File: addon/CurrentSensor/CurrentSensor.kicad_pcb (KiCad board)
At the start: 2 copper layers, 25.5 x 14 mm, 3 parts, among them J102 Conn_01x08_Male, J103 Conn_01x08_Male

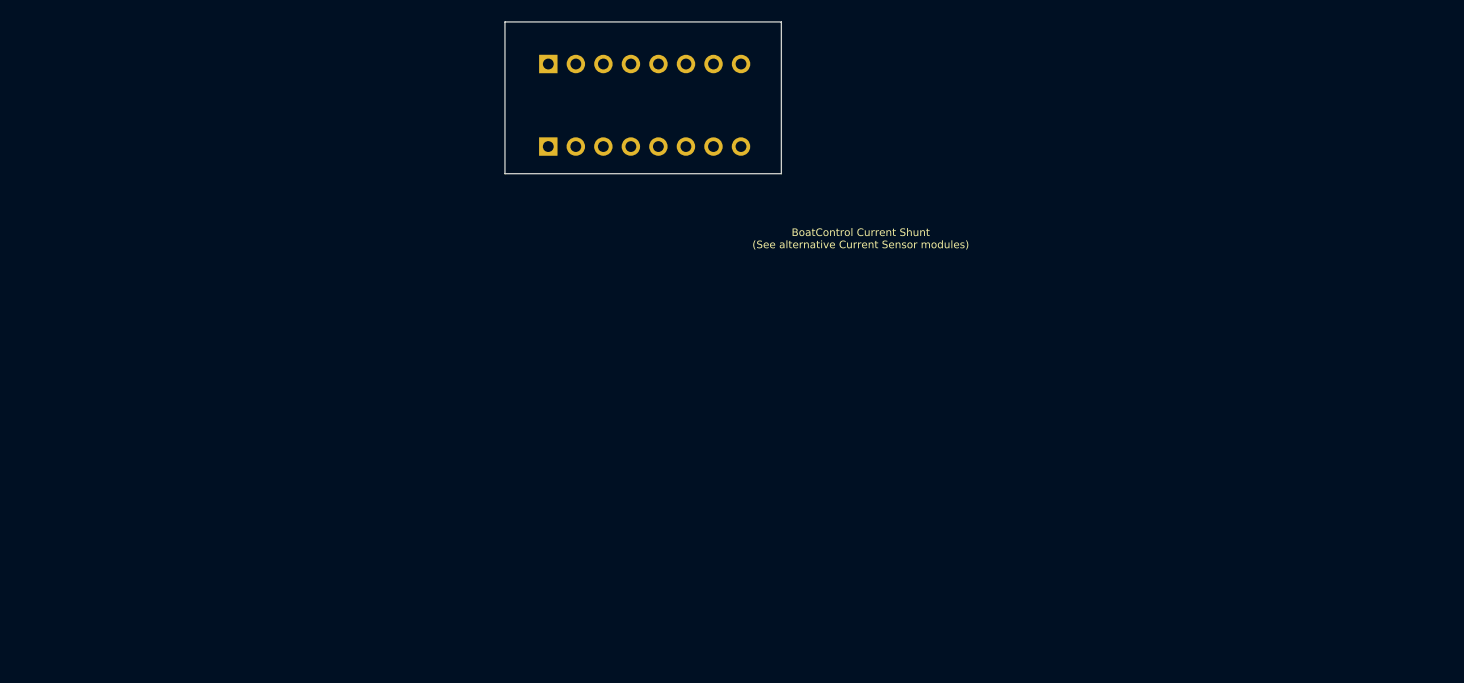
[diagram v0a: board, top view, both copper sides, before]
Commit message: Fix power interconnects
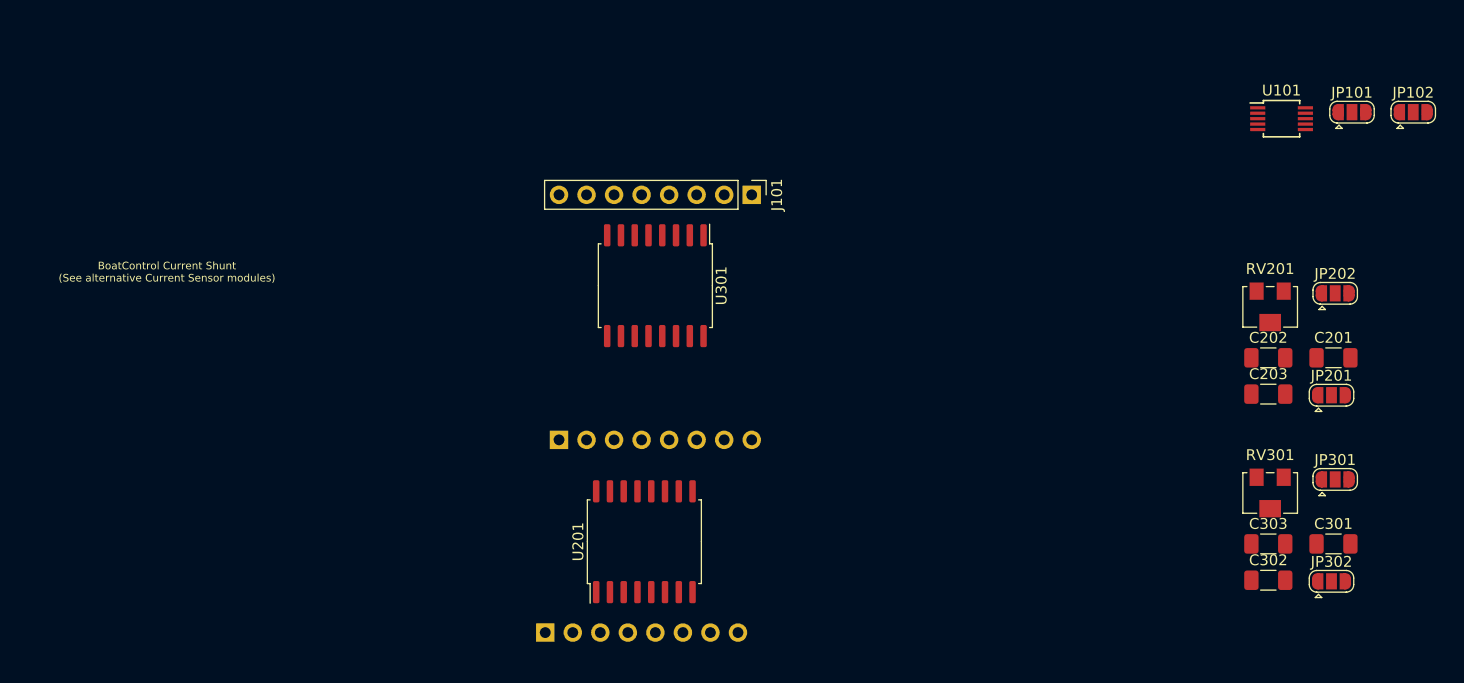
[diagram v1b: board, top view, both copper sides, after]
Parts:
- added C201: 0.1uF, Capacitor_SMD:C_1206_3216Metric_Pad1.33x1.80mm_HandSolder, F.Cu at (213.4, 123.0)
- added C202: 10uF, Capacitor_SMD:C_1206_3216Metric_Pad1.33x1.80mm_HandSolder, F.Cu at (207.4, 123.0)
- added C203: 0.1nF, Capacitor_SMD:C_1206_3216Metric_Pad1.33x1.80mm_HandSolder, F.Cu at (207.4, 126.3)
- added C301: 0.1uF, Capacitor_SMD:C_1206_3216Metric_Pad1.33x1.80mm_HandSolder, F.Cu at (213.4, 140.2)
- added C302: 10uF, Capacitor_SMD:C_1206_3216Metric_Pad1.33x1.80mm_HandSolder, F.Cu at (207.4, 143.5)
- added C303: 0.1nF, Capacitor_SMD:C_1206_3216Metric_Pad1.33x1.80mm_HandSolder, F.Cu at (207.4, 140.2)
- added J101: Conn_01x08_Male, Connector_PinHeader_2.54mm:PinHeader_1x08_P2.54mm_Vertical, F.Cu at (159.8, 108.0)
- added JP101: SolderJumper_3_Open, Jumper:SolderJumper-3_P1.3mm_Open_RoundedPad1.0x1.5mm, F.Cu at (215.1, 100.3)
- added JP102: SolderJumper_3_Open, Jumper:SolderJumper-3_P1.3mm_Open_RoundedPad1.0x1.5mm, F.Cu at (220.8, 100.3)
- added JP201: SolderJumper_3_Open, Jumper:SolderJumper-3_P1.3mm_Open_RoundedPad1.0x1.5mm, F.Cu at (213.3, 126.4)
- added JP202: SolderJumper_3_Open, Jumper:SolderJumper-3_P1.3mm_Open_RoundedPad1.0x1.5mm, F.Cu at (213.6, 117.0)
- added JP301: SolderJumper_3_Open, Jumper:SolderJumper-3_P1.3mm_Open_RoundedPad1.0x1.5mm, F.Cu at (213.6, 134.2)
- added JP302: SolderJumper_3_Open, Jumper:SolderJumper-3_P1.3mm_Open_RoundedPad1.0x1.5mm, F.Cu at (213.3, 143.6)
- added RV201: 50K Ω Trimpot, Potentiometer_SMD:Potentiometer_Bourns_3214W_Vertical, F.Cu at (207.6, 118.3)
- added RV301: 50K Ω Trimpot, Potentiometer_SMD:Potentiometer_Bourns_3214W_Vertical, F.Cu at (207.6, 135.5)
- added U101: MCP3423, Package_SO:MSOP-10_3x3mm_P0.5mm, F.Cu at (208.6, 100.9)
- added U201: ACS37002, Package_SO:SOIC-16W_7.5x10.3mm_P1.27mm, F.Cu at (149.9, 140.0)
- added U301: ACS37002, Package_SO:SOIC-16W_7.5x10.3mm_P1.27mm, F.Cu at (150.9, 116.3)
- moved J103 44.8 mm to (140.7, 148.3)
- moved J102 34.7 mm to (142.0, 130.6)
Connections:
- net /Power renamed /Sensor 1/IP+
- net Net-(J103-Pad5) renamed /Sensor 1/IP-
- J102 pad 1: (no net) -> Net-(J102-Pad1)
- J102 pad 2: (no net) -> Net-(J102-Pad1)
- J102 pad 3: (no net) -> Net-(J102-Pad3)
- J102 pad 4: (no net) -> Net-(J102-Pad3)
- J102 pad 5: (no net) -> Net-(J102-Pad5)
- J102 pad 6: (no net) -> Net-(J102-Pad6)
- J102 pad 7: (no net) -> /Sensor 2/OCF
- J102 pad 8: (no net) -> /Sensor 1/OCF
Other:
- board outline removed

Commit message: Park Current Sensing
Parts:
- moved RV301 47.0 mm to (160.8, 139.4)
- moved C201 41.7 mm to (171.8, 125.3)
- moved C202 41.7 mm to (165.8, 125.3)
- moved C301 41.3 mm to (173.1, 131.5)
- moved C303 41.3 mm to (167.0, 131.5)
- moved RV201 38.3 mm to (169.4, 115.1)
- moved C302 36.8 mm to (170.9, 138.7)
- moved JP302 34.5 mm to (179.2, 149.4)
- moved C203 31.5 mm to (178.1, 137.7)
- moved J101 4.60 mm to (160.3, 112.5)
- moved U301 4.60 mm to (151.4, 120.9)
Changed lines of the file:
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@@
   )
   (module Package_SO:SOIC-16W_7.5x10.3mm_P1.27mm (layer F.Cu)
-    (at 150.876 116.332 270)
+    (at 151.384 120.904 270)
     (descr "SOIC, 16 Pin (JEDEC MS-013AA, https://www.analog.com/media/en/package-pcb-resources/package/pkg_pdf/soic_wide-rw/rw_16.pdf), generated with kicad-footprint-generator ipc_gullwing_generator.py")
     (tags "SOIC SO")
@@
   )
   (module Potentiometer_SMD:Potentiometer_Bourns_3214W_Vertical (layer F.Cu)
-    (at 207.5962 135.4568)
+    (at 160.782 139.446)
     (descr "Potentiometer, vertical, Bourns 3214W, https://www.bourns.com/docs/Product-Datasheets/3214.pdf")
     (tags "Potentiometer vertical Bourns 3214W")
@@
   )
   (module Potentiometer_SMD:Potentiometer_Bourns_3214W_Vertical (layer F.Cu)
-    (at 207.5962 118.2868)
+    (at 169.418 115.062)
     (descr "Potentiometer, vertical, Bourns 3214W, https://www.bourns.com/docs/Product-Datasheets/3214.pdf")
     (tags "Potentiometer vertical Bourns 3214W")
@@
   )
   (module Jumper:SolderJumper-3_P1.3mm_Open_RoundedPad1.0x1.5mm (layer F.Cu)
-    (at 213.2562 143.6068)
+    (at 179.2202 149.4488)
     (descr "SMD Solder 3-pad Jumper, 1x1.5mm rounded Pads, 0.3mm gap, open")
     (tags "solder jumper open")
@@
   )
   (module Connector_PinHeader_2.54mm:PinHeader_1x08_P2.54mm_Vertical (layer F.Cu)
-    (at 159.766 107.95 270)
+    (at 160.274 112.522 270)
     (descr "Through hole straight pin header, 1x08, 2.54mm pitch, single row")
     (tags "Through hole pin header THT 1x08 2.54mm single row")
@@
   )
   (module Capacitor_SMD:C_1206_3216Metric_Pad1.33x1.80mm_HandSolder (layer F.Cu)
-    (at 207.4262 140.1568)
+    (at 167.0402 131.5208)
     (descr "Capacitor SMD 1206 (3216 Metric), square (rectangular) end terminal, IPC_7351 nominal with elongated pad for handsoldering. (Body size source: IPC-SM-782 page 76, https://www.pcb-3d.com/wordpress/wp-content/uploads/ipc-sm-782a_amendment_1_and_2.pdf), generated with kicad-footprint-generator")
     (tags "capacitor handsolder")
@@
   )
   (module Capacitor_SMD:C_1206_3216Metric_Pad1.33x1.80mm_HandSolder (layer F.Cu)
-    (at 207.4262 143.5068)
+    (at 170.942 138.684)
     (descr "Capacitor SMD 1206 (3216 Metric), square (rectangular) end terminal, IPC_7351 nominal with elongated pad for handsoldering. (Body size source: IPC-SM-782 page 76, https://www.pcb-3d.com/wordpress/wp-content/uploads/ipc-sm-782a_amendment_1_and_2.pdf), generated with kicad-footprint-generator")
     (tags "capacitor handsolder")
@@
   )
   (module Capacitor_SMD:C_1206_3216Metric_Pad1.33x1.80mm_HandSolder (layer F.Cu)
-    (at 213.4362 140.1568)
+    (at 173.0502 131.5208)
     (descr "Capacitor SMD 1206 (3216 Metric), square (rectangular) end terminal, IPC_7351 nominal with elongated pad for handsoldering. (Body size source: IPC-SM-782 page 76, https://www.pcb-3d.com/wordpress/wp-content/uploads/ipc-sm-782a_amendment_1_and_2.pdf), generated with kicad-footprint-generator")
     (tags "capacitor handsolder")
@@
   )
   (module Capacitor_SMD:C_1206_3216Metric_Pad1.33x1.80mm_HandSolder (layer F.Cu)
-    (at 207.4262 126.3368)
+    (at 178.054 137.668)
     (descr "Capacitor SMD 1206 (3216 Metric), square (rectangular) end terminal, IPC_7351 nominal with elongated pad for handsoldering. (Body size source: IPC-SM-782 page 76, https://www.pcb-3d.com/wordpress/wp-content/uploads/ipc-sm-782a_amendment_1_and_2.pdf), generated with kicad-footprint-generator")
     (tags "capacitor handsolder")
@@
   )
   (module Capacitor_SMD:C_1206_3216Metric_Pad1.33x1.80mm_HandSolder (layer F.Cu)
-    (at 207.4262 122.9868)
+    (at 165.7702 125.2728)
     (descr "Capacitor SMD 1206 (3216 Metric), square (rectangular) end terminal, IPC_7351 nominal with elongated pad for handsoldering. (Body size source: IPC-SM-782 page 76, https://www.pcb-3d.com/wordpress/wp-content/uploads/ipc-sm-782a_amendment_1_and_2.pdf), generated with kicad-footprint-generator")
     (tags "capacitor handsolder")
@@
   )
   (module Capacitor_SMD:C_1206_3216Metric_Pad1.33x1.80mm_HandSolder (layer F.Cu)
-    (at 213.4362 122.9868)
+    (at 171.7802 125.2728)
     (descr "Capacitor SMD 1206 (3216 Metric), square (rectangular) end terminal, IPC_7351 nominal with elongated pad for handsoldering. (Body size source: IPC-SM-782 page 76, https://www.pcb-3d.com/wordpress/wp-content/uploads/ipc-sm-782a_amendment_1_and_2.pdf), generated with kicad-footprint-generator")
     (tags "capacitor handsolder")
